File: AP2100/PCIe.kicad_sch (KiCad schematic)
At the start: 3 parts, among them J1 Bus_PCI_Express_Mini, J2 Bus_PCI_Express_Mini, J3 Bus_PCI_Express_Mini

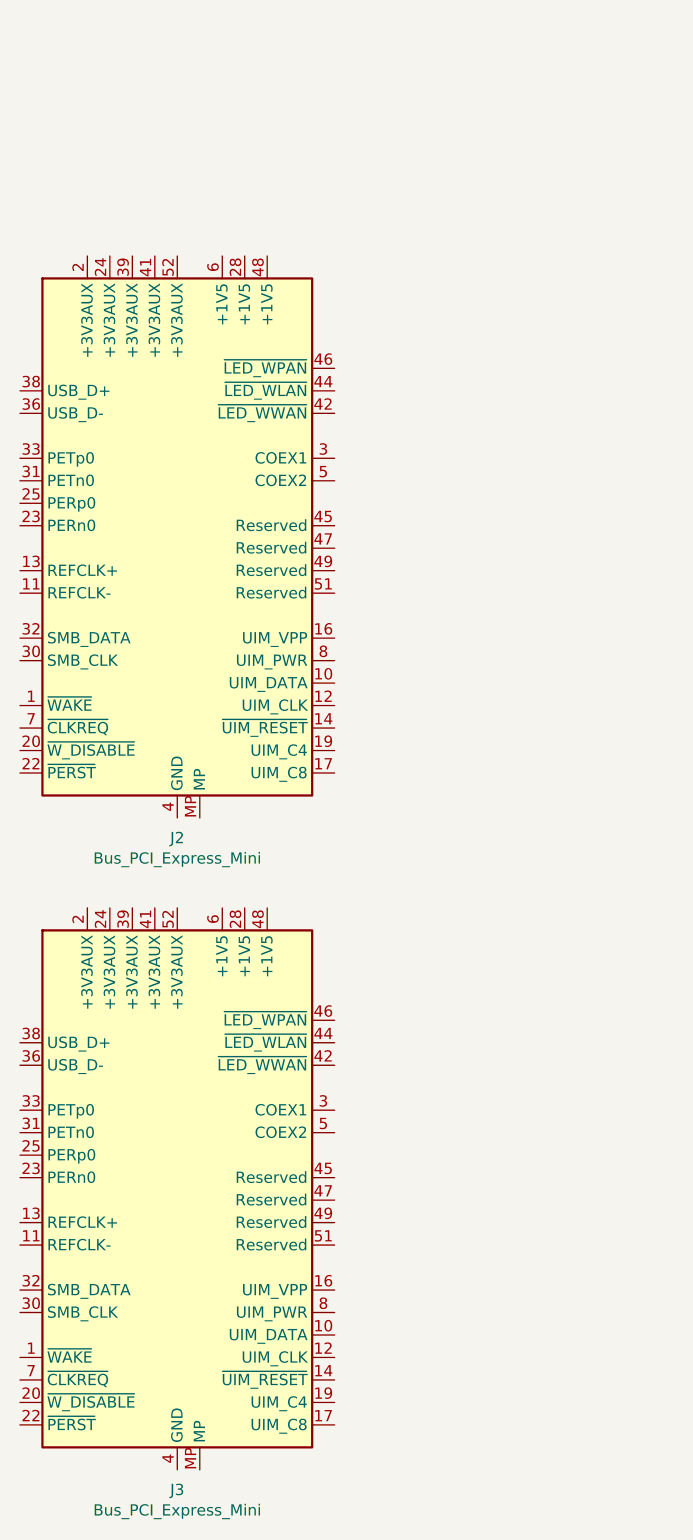
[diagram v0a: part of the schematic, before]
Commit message: Add clocking and start of ethernet
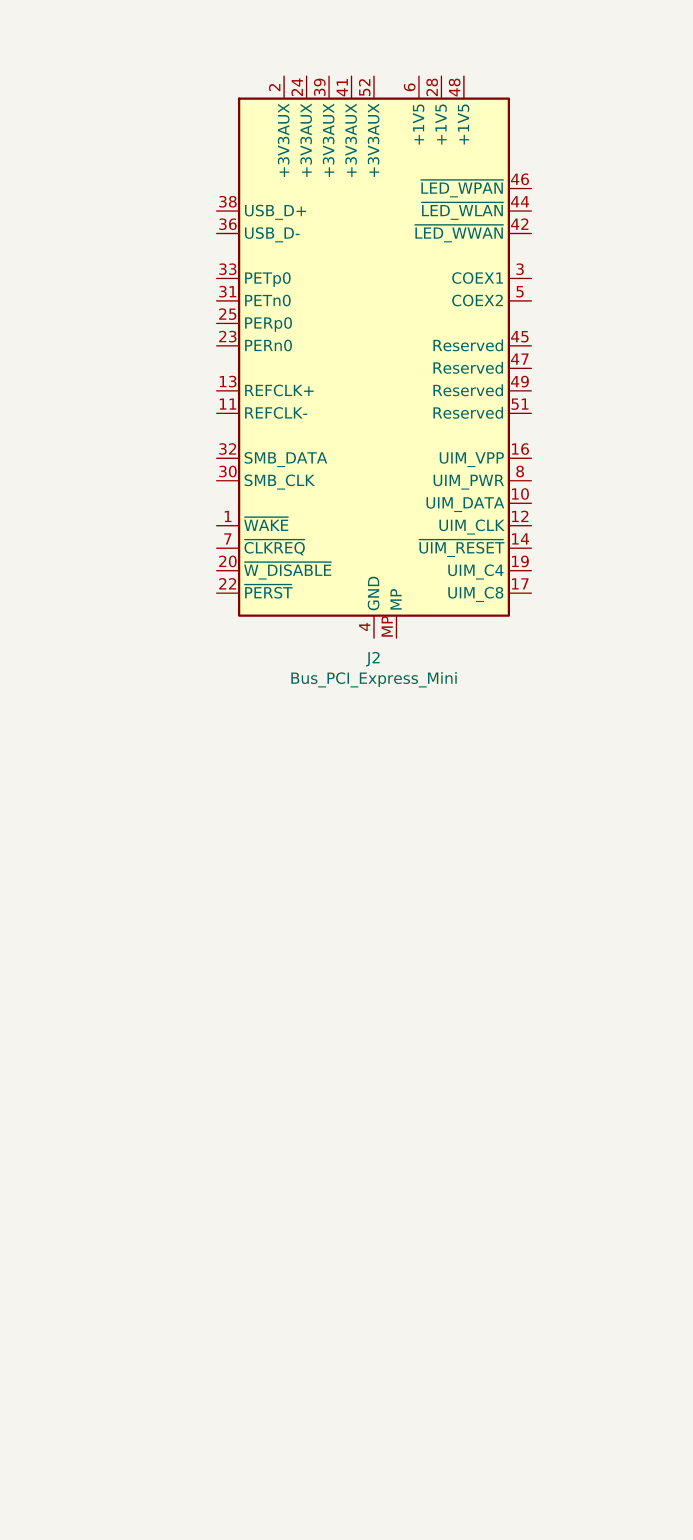
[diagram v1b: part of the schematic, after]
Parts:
- removed J3: Bus_PCI_Express_Mini, Connector_PCBEdge:BUS_PCI_Express_Mini_Full, symbol Connector:Bus_PCI_Express_Mini
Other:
- moved on the sheet: J2
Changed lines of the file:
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@@
 (kicad_sch (version 20200828) (generator eeschema)
-  (page 9 9)
-  (paper "USLegal")
+  (page 8 9)
+  (paper "A3")
   (title_block
     (title "AP2100")
     (company "IS ImageStream Internet Solutions, Inc.")
   )
-  (symbol (lib_id "Connector:Bus_PCI_Express_Mini") (at 50.8 85.09 0) (unit 1)
+  (symbol (lib_id "Connector:Bus_PCI_Express_Mini") (at 73.025 64.77 0)
     (in_bom yes) (on_board yes)
-    (property "Reference" "J2" (id 0) (at 50.8 117.8306 0))
-    (property "Value" "Bus_PCI_Express_Mini" (id 1) (at 50.8 120.142 0))
-    (property "Footprint" "Connector_PCBEdge:BUS_PCI_Express_Mini_Full" (id 2) (at 50.8 85.09 0)
+    (property "Reference" "J2" (id 0) (at 73.025 97.5106 0))
+    (property "Value" "Bus_PCI_Express_Mini" (id 1) (at 73.025 99.822 0))
+    (property "Footprint" "Connector_PCBEdge:BUS_PCI_Express_Mini_Full" (id 2) (at 73.025 64.77 0)
       (effects (font (size 1.27 1.27)) hide)
     )
-    (property "Datasheet" "~" (id 3) (at 46.99 114.3 0)
+    (property "Datasheet" "~" (id 3) (at 69.215 93.98 0)
       (effects (font (size 1.27 1.27)) hide)
     )
-    (property "MFR" "-" (id 4) (at 0 170.18 0)
+    (property "MFR" "-" (id 4) (at 22.225 149.86 0)
       (effects (font (size 1.27 1.27)) hide)
     )
-    (property "MPN" "-" (id 5) (at 0 170.18 0)
+    (property "MPN" "-" (id 5) (at 22.225 149.86 0)
       (effects (font (size 1.27 1.27)) hide)
     )
-    (property "SPR" "-" (id 6) (at 0 170.18 0)
+    (property "SPR" "-" (id 6) (at 22.225 149.86 0)
       (effects (font (size 1.27 1.27)) hide)
     )
-    (property "SPN" "-" (id 7) (at 0 170.18 0)
+    (property "SPN" "-" (id 7) (at 22.225 149.86 0)
       (effects (font (size 1.27 1.27)) hide)
     )
-    (property "SPURL" "-" (id 8) (at 0 170.18 0)
+    (property "SPURL" "-" (id 8) (at 22.225 149.86 0)
       (effects (font (size 1.27 1.27)) hide)
     )
   )
-  (symbol (lib_id "Connector:Bus_PCI_Express_Mini") (at 50.8 158.75 0) (unit 1)
-    (in_bom yes) (on_board yes)
-    (property "Reference" "J3" (id 0) (at 50.8 191.4906 0))
-    (property "Value" "Bus_PCI_Express_Mini" (id 1) (at 50.8 193.802 0))
-    (property "Footprint" "Connector_PCBEdge:BUS_PCI_Express_Mini_Full" (id 2) (at 50.8 158.75 0)
-      (effects (font (size 1.27 1.27)) hide)
-    )
-    (property "Datasheet" "~" (id 3) (at 46.99 187.96 0)
-      (effects (font (size 1.27 1.27)) hide)
-    )
-    (property "MFR" "-" (id 4) (at 0 317.5 0)
-      (effects (font (size 1.27 1.27)) hide)
-    )
-    (property "MPN" "-" (id 5) (at 0 317.5 0)
-      (effects (font (size 1.27 1.27)) hide)
-    )
-    (property "SPR" "-" (id 6) (at 0 317.5 0)
-      (effects (font (size 1.27 1.27)) hide)
-    )
-    (property "SPN" "-" (id 7) (at 0 317.5 0)
-      (effects (font (size 1.27 1.27)) hide)
-    )
-    (property "SPURL" "-" (id 8) (at 0 317.5 0)
-      (effects (font (size 1.27 1.27)) hide)
-    )
-  )
-  (symbol (lib_id "Connector:Bus_PCI_Express_Mini") (at 231.14 58.42 0) (unit 1)
+  (symbol (lib_id "Connector:Bus_PCI_Express_Mini") (at 231.14 58.42 0)
     (in_bom yes) (on_board yes)
     (property "Reference" "J1" (id 0) (at 231.14 91.1606 0))

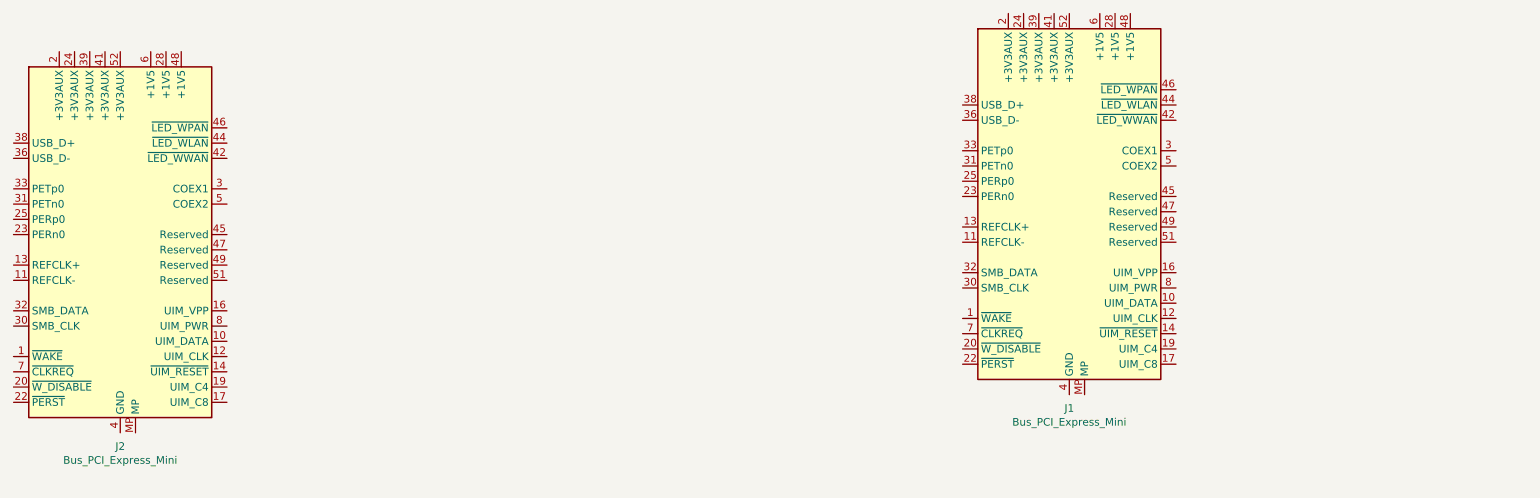
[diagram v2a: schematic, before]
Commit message: Mostly done with USB - USB1 complete just duplicate to 2+3
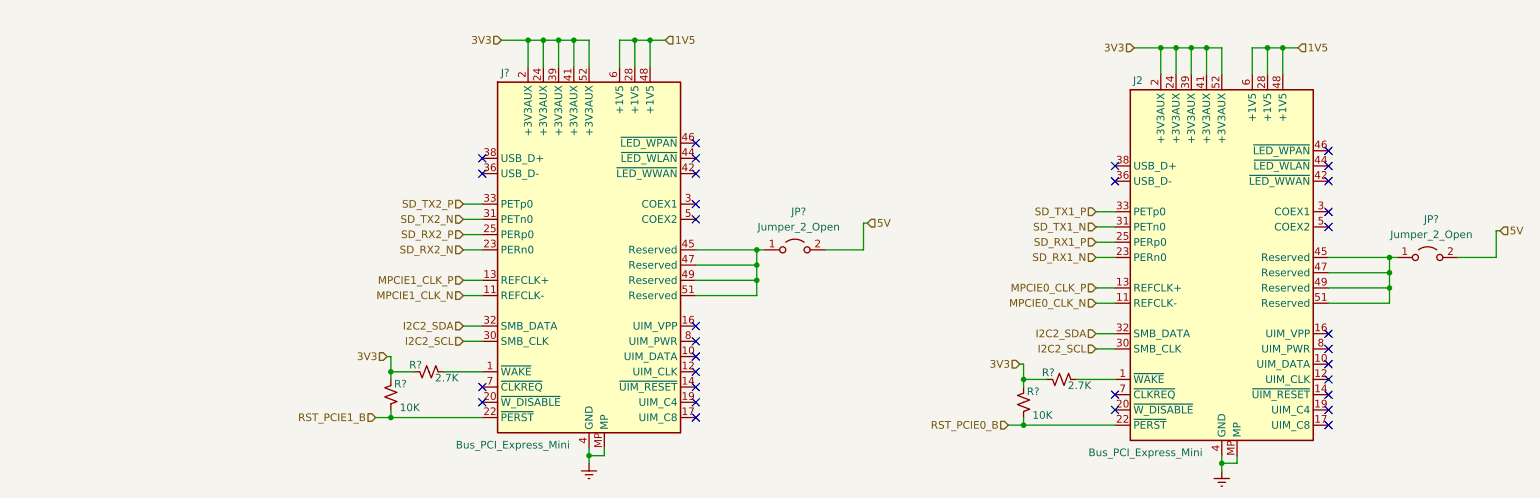
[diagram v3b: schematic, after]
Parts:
- removed J1: Bus_PCI_Express_Mini, Connector_PCBEdge:BUS_PCI_Express_Mini_Full, symbol Connector:Bus_PCI_Express_Mini
- added J?: Bus_PCI_Express_Mini, Connector_PCBEdge:BUS_PCI_Express_Mini_Full, symbol Connector:Bus_PCI_Express_Mini
- added JP? (x2): Jumper_2_Open, Connector_PinHeader_2.54mm:PinHeader_1x02_P2.54mm_Vertical, symbol Jumper:Jumper_2_Open
- added R? (x2): 2.7K, Resistor_SMD:R_0402_1005Metric, symbol Device:R_Small_US
- added R? (x2): 10K, Resistor_SMD:R_0402_1005Metric, symbol Device:R_Small_US
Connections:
- net at J2.1 (~WAKE): now also R?.1
- net MPCIE0_CLK_N: now reaches J2.11 (REFCLK-)
- net MPCIE0_CLK_P: now reaches J2.13 (REFCLK+)
- net GND: now reaches J2.15 (GND), J2.18 (GND), J2.21 (GND), J2.26 (GND), J2.27 (GND), J2.29 (GND), J2.34 (GND), J2.35 (GND), J2.37 (GND), J2.4 (GND), J2.40 (GND), J2.43 (GND), J2.50 (GND), J2.9 (GND)
- net GND: now also J2.MP, J?.15 (GND), J?.18 (GND), J?.21 (GND), J?.26 (GND), J?.27 (GND), J?.29 (GND), J?.34 (GND), J?.35 (GND), J?.37 (GND), J?.4 (GND), J?.40 (GND), J?.43 (GND), J?.50 (GND), J?.9 (GND), J?.MP
- net 3V3: now reaches J2.2 (+3V3AUX)
- net 3V3: now also J2.24 (+3V3AUX), J2.39 (+3V3AUX), J2.41 (+3V3AUX), J2.52 (+3V3AUX), J?.2 (+3V3AUX), J?.24 (+3V3AUX), J?.39 (+3V3AUX), J?.41 (+3V3AUX), J?.52 (+3V3AUX), R?.1, R?.1, R?.2, R?.2
- net RST_PCIE0_B: now reaches J2.22 (~PERST)
- net RST_PCIE0_B: now also R?.2
- net SD_RX1_N: now reaches J2.23 (PERn0)
- net SD_RX1_P: now reaches J2.25 (PERp0)
- net 1V5: now reaches J2.28 (+1V5)
- net 1V5: now also J2.48 (+1V5), J2.6 (+1V5), J?.28 (+1V5), J?.48 (+1V5), J?.6 (+1V5)
- net I2C2_SCL: now reaches J2.30 (SMB_CLK)
- net I2C2_SCL: now also J?.30 (SMB_CLK)
- net SD_TX1_N: now reaches J2.31 (PETn0)
- net I2C2_SDA: now reaches J2.32 (SMB_DATA)
- net I2C2_SDA: now also J?.32 (SMB_DATA)
- net SD_TX1_P: now reaches J2.33 (PETp0)
- net at J2.45 (Reserved): now also J2.47 (Reserved), J2.49 (Reserved), J2.51 (Reserved), JP?.1 (A)
- new net: J?.45 (Reserved), J?.47 (Reserved), J?.49 (Reserved), J?.51 (Reserved), JP?.1 (A)
- new net: J?.1 (~WAKE), R?.1
- new net 5V: JP?.2 (B), JP?.2 (B)
- new net MPCIE1_CLK_N: J?.11 (REFCLK-)
- new net MPCIE1_CLK_P: J?.13 (REFCLK+)
- new net RST_PCIE1_B: J?.22 (~PERST), R?.2
- new net SD_RX2_N: J?.23 (PERn0)
- new net SD_RX2_P: J?.25 (PERp0)
- new net SD_TX2_N: J?.31 (PETn0)
- new net SD_TX2_P: J?.33 (PETp0)
- no-connect marks 0 -> 32
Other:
- moved on the sheet: J2

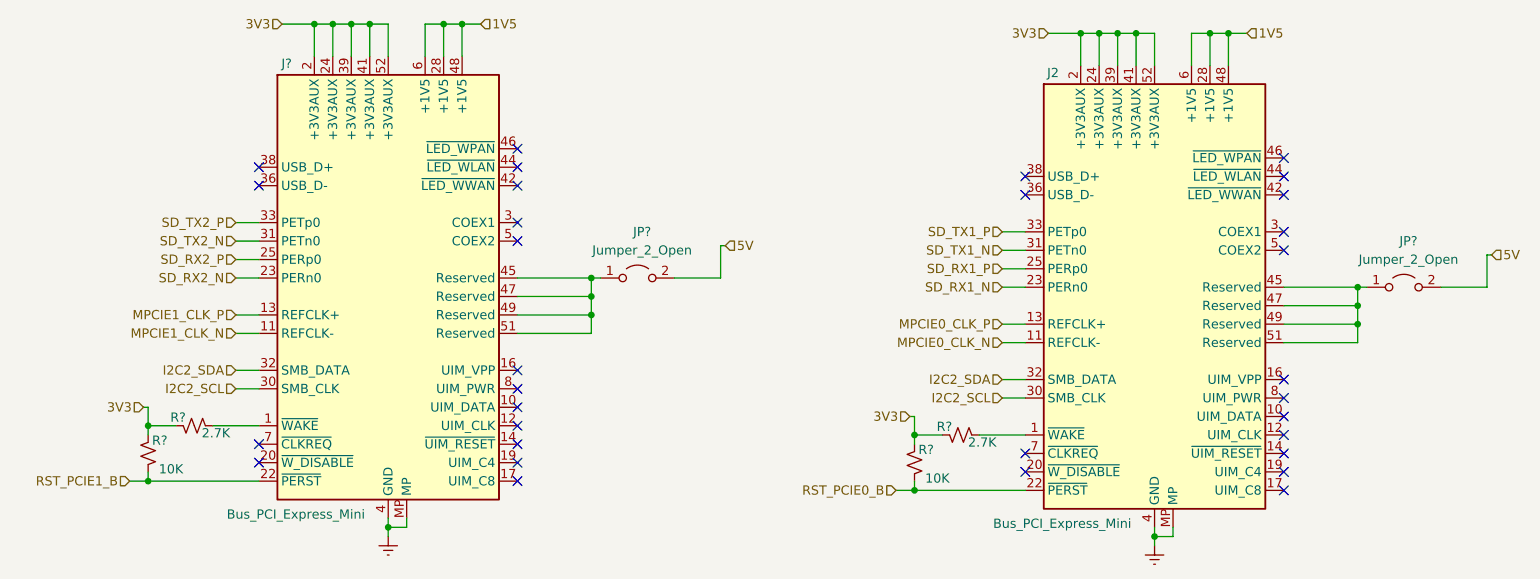
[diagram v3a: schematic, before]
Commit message: Annotate and update PCB with current design
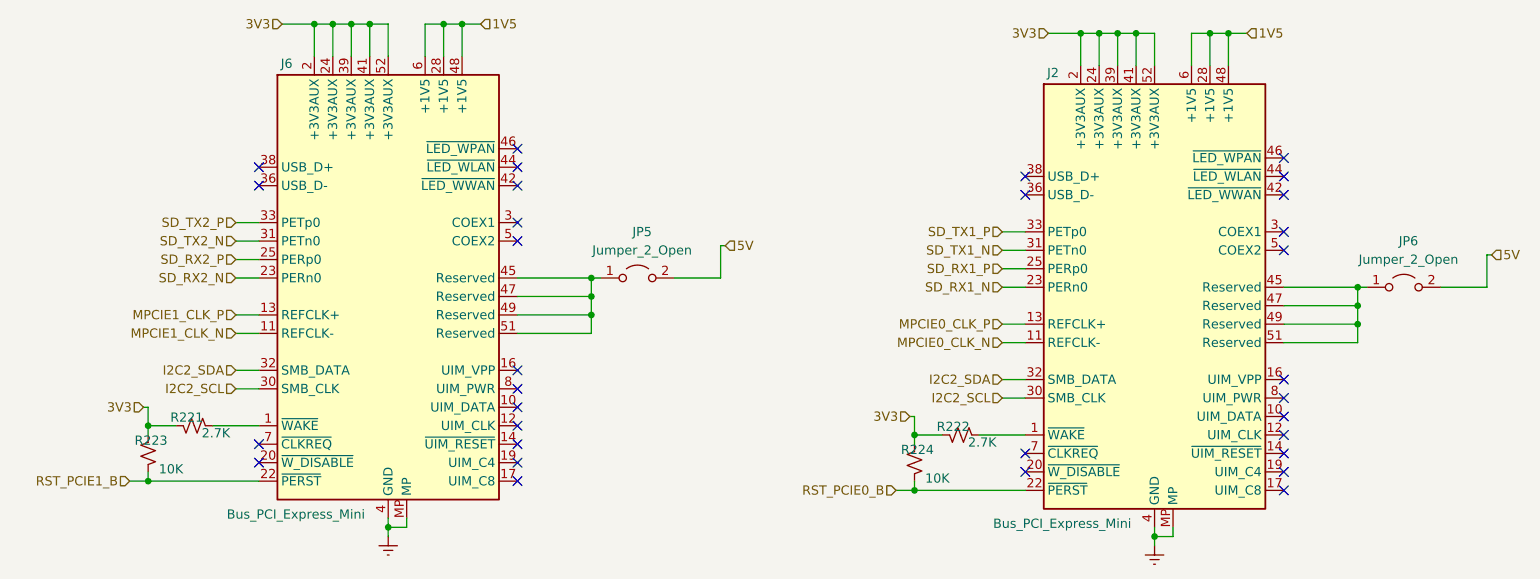
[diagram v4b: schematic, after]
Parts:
- gave numbers to parts that had none: 7
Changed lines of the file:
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@@
   (symbol (lib_id "AP2100-rescue:GND-Scott") (at 151.13 100.33 0) (mirror y) (unit 1)
     (in_bom yes) (on_board yes)
-    (property "Reference" "#PWR?" (id 0) (at 151.13 106.68 0)
+    (property "Reference" "#PWR0255" (id 0) (at 151.13 106.68 0)
       (effects (font (size 1.27 1.27)) hide)
     )
@@
   (symbol (lib_id "AP2100-rescue:GND-Scott") (at 256.54 101.6 0) (mirror y) (unit 1)
     (in_bom yes) (on_board yes)
-    (property "Reference" "#PWR?" (id 0) (at 256.54 107.95 0)
+    (property "Reference" "#PWR0254" (id 0) (at 256.54 107.95 0)
       (effects (font (size 1.27 1.27)) hide)
     )
@@
   (symbol (lib_id "Device:R_Small_US") (at 118.11 88.9 0) (mirror y) (unit 1)
     (in_bom yes) (on_board yes)
-    (property "Reference" "R?" (id 0) (at 120.777 87.122 0)
+    (property "Reference" "R223" (id 0) (at 120.777 87.122 0)
       (effects (font (size 1.27 1.27)) (justify left))
     )
@@
   (symbol (lib_id "Device:R_Small_US") (at 124.46 85.09 270) (mirror x) (unit 1)
     (in_bom yes) (on_board yes)
-    (property "Reference" "R?" (id 0) (at 121.158 83.947 90)
+    (property "Reference" "R221" (id 0) (at 121.158 83.947 90)
       (effects (font (size 1.27 1.27)) (justify left))
     )
@@
   (symbol (lib_id "Device:R_Small_US") (at 223.52 90.17 0) (mirror y) (unit 1)
     (in_bom yes) (on_board yes)
-    (property "Reference" "R?" (id 0) (at 226.187 88.392 0)
+    (property "Reference" "R224" (id 0) (at 226.187 88.392 0)
       (effects (font (size 1.27 1.27)) (justify left))
     )
@@
   (symbol (lib_id "Device:R_Small_US") (at 229.87 86.36 270) (mirror x) (unit 1)
     (in_bom yes) (on_board yes)
-    (property "Reference" "R?" (id 0) (at 226.568 85.217 90)
+    (property "Reference" "R222" (id 0) (at 226.568 85.217 90)
       (effects (font (size 1.27 1.27)) (justify left))
     )
@@
   (symbol (lib_id "Jumper:Jumper_2_Open") (at 185.42 64.77 0) (unit 1)
     (in_bom yes) (on_board yes)
-    (property "Reference" "JP?" (id 0) (at 186.055 58.42 0))
+    (property "Reference" "JP5" (id 0) (at 186.055 58.42 0))
     (property "Value" "Jumper_2_Open" (id 1) (at 186.055 60.96 0))
     (property "Footprint" "Connector_PinHeader_2.54mm:PinHeader_1x02_P2.54mm_Vertical" (id 2) (at 185.42 64.77 0)
@@
   (symbol (lib_id "Jumper:Jumper_2_Open") (at 290.83 66.04 0) (unit 1)
     (in_bom yes) (on_board yes)
-    (property "Reference" "JP?" (id 0) (at 291.465 59.69 0))
+    (property "Reference" "JP6" (id 0) (at 291.465 59.69 0))
     (property "Value" "Jumper_2_Open" (id 1) (at 291.465 62.23 0))
     (property "Footprint" "Connector_PinHeader_2.54mm:PinHeader_1x02_P2.54mm_Vertical" (id 2) (at 290.83 66.04 0)
@@
   (symbol (lib_id "Connector:Bus_PCI_Express_Mini") (at 151.13 67.31 0) (unit 1)
     (in_bom yes) (on_board yes)
-    (property "Reference" "J?" (id 0) (at 137.16 35.2806 0))
+    (property "Reference" "J6" (id 0) (at 137.16 35.2806 0))
     (property "Value" "Bus_PCI_Express_Mini" (id 1) (at 138.43 97.282 0))
     (property "Footprint" "Connector_PCBEdge:BUS_PCI_Express_Mini_Full" (id 2) (at 151.13 67.31 0)
